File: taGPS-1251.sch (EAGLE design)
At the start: 84 parts, among them IC1 MSP430FR698X(1)80-PIN_PN, IC3 FT232RL

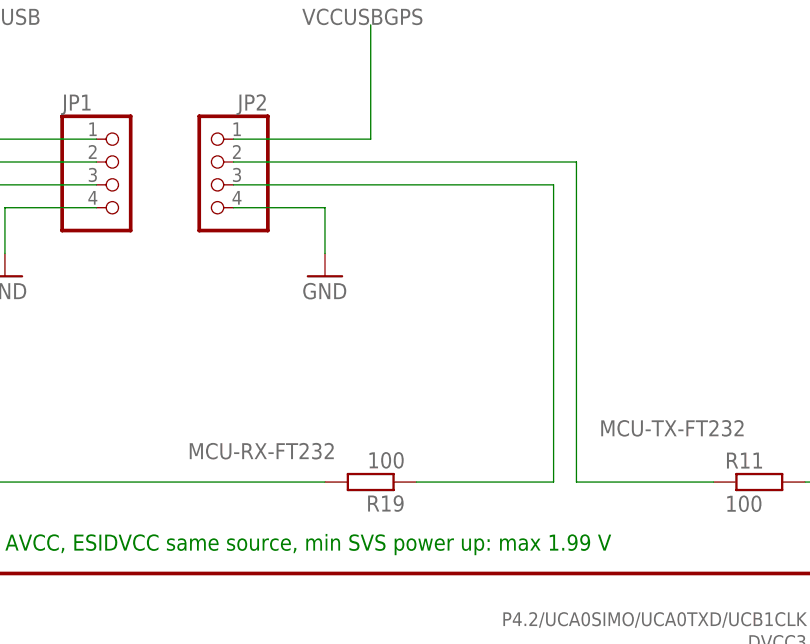
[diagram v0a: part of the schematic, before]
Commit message: Fix MCU RX/TX pinheader position, polish boards
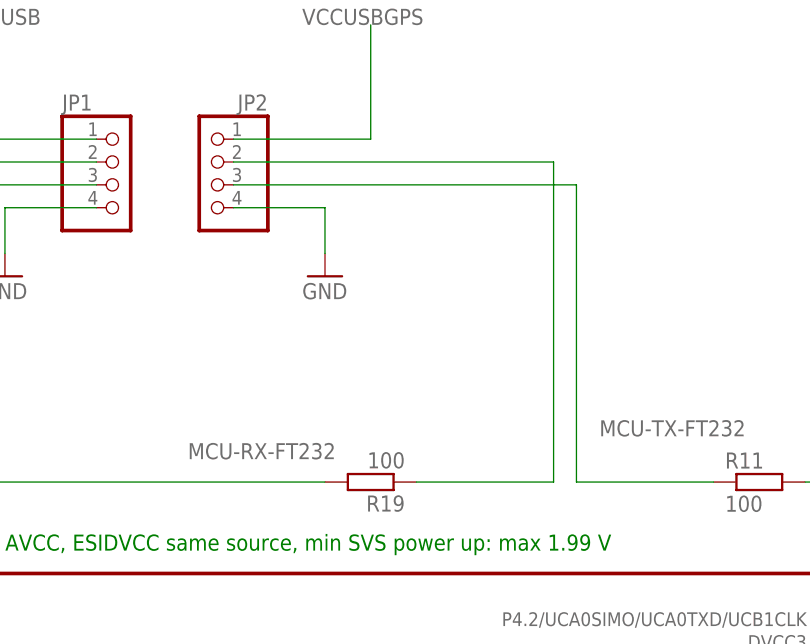
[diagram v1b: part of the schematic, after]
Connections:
- net MCU-TX-FT232: now also JP2.3; no longer JP2.2
- net N$8: now also JP2.2; no longer JP2.3
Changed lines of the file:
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@@
 <label x="-38.1" y="45.72" size="1.778" layer="95"/>
 <wire x1="-25.4" y1="40.64" x2="-40.64" y2="40.64" width="0.1524" layer="91"/>
-<wire x1="-40.64" y1="40.64" x2="-40.64" y2="76.2" width="0.1524" layer="91"/>
-<pinref part="JP2" gate="A" pin="2"/>
-<wire x1="-40.64" y1="76.2" x2="-78.74" y2="76.2" width="0.1524" layer="91"/>
+<wire x1="-40.64" y1="40.64" x2="-40.64" y2="73.66" width="0.1524" layer="91"/>
+<pinref part="JP2" gate="A" pin="3"/>
+<wire x1="-78.74" y1="73.66" x2="-40.64" y2="73.66" width="0.1524" layer="91"/>
 </segment>
 </net>
@@
 <pinref part="R19" gate="G$1" pin="1"/>
 <wire x1="-58.42" y1="40.64" x2="-43.18" y2="40.64" width="0.1524" layer="91"/>
-<wire x1="-43.18" y1="40.64" x2="-43.18" y2="73.66" width="0.1524" layer="91"/>
-<pinref part="JP2" gate="A" pin="3"/>
-<wire x1="-43.18" y1="73.66" x2="-78.74" y2="73.66" width="0.1524" layer="91"/>
-</segment>
-</net>
+<wire x1="-43.18" y1="40.64" x2="-43.18" y2="76.2" width="0.1524" layer="91"/>
+<pinref part="JP2" gate="A" pin="2"/>
+<wire x1="-43.18" y1="76.2" x2="-78.74" y2="76.2" width="0.1524" layer="91"/>
+</segment>
+</net>

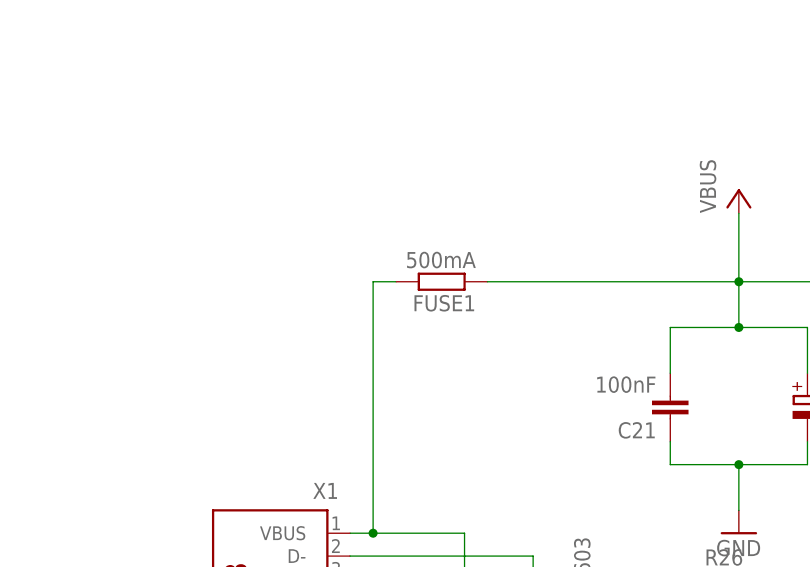
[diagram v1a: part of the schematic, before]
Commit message: Replace FUSE package to 1812
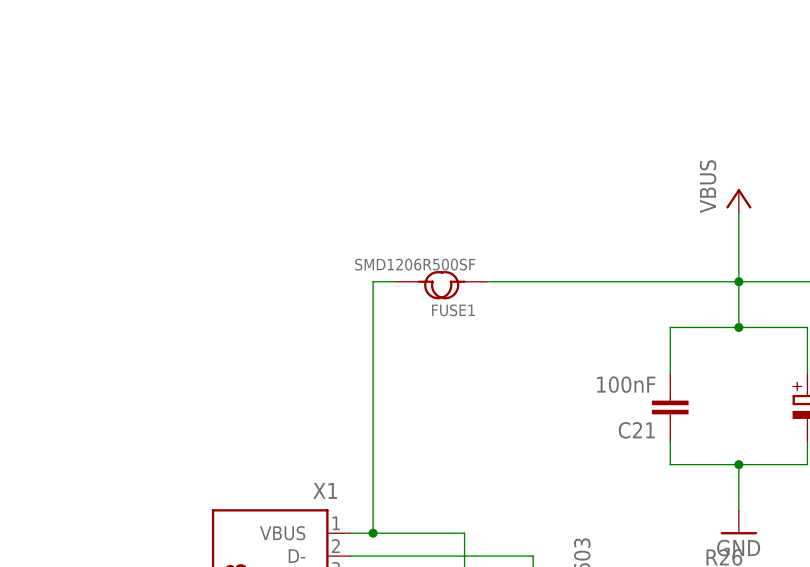
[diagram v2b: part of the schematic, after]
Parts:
- FUSE1: value 500mA -> SMD1206R500SF; device tagps:R-EU_R0805 -> tagps:SMD-PPTC-500MA-15V(1812)
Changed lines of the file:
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@@
 <layer number="48" name="Document" color="7" fill="1" visible="no" active="no"/>
 <layer number="49" name="Reference" color="7" fill="1" visible="no" active="no"/>
+<layer number="50" name="dxf" color="7" fill="1" visible="no" active="no"/>
 <layer number="51" name="tDocu" color="7" fill="1" visible="no" active="no"/>
 <layer number="52" name="bDocu" color="7" fill="1" visible="no" active="no"/>
+<layer number="53" name="tGND_GNDA" color="7" fill="9" visible="no" active="no"/>
+<layer number="54" name="bGND_GNDA" color="1" fill="9" visible="no" active="no"/>
+<layer number="56" name="wert" color="7" fill="1" visible="no" active="no"/>
+<layer number="57" name="tCAD" color="7" fill="1" visible="no" active="no"/>
 <layer number="90" name="Modules" color="5" fill="1" visible="yes" active="yes"/>
 <layer number="91" name="Nets" color="2" fill="1" visible="yes" active="yes"/>
@@
 <layer number="98" name="Guide" color="6" fill="1" visible="yes" active="yes"/>
 <layer number="99" name="SpiceOrder" color="5" fill="1" visible="yes" active="yes"/>
+<layer number="100" name="Muster" color="7" fill="1" visible="no" active="no"/>
+<layer number="101" name="Patch_Top" color="12" fill="4" visible="no" active="no"/>
+<layer number="102" name="Vscore" color="7" fill="1" visible="no" active="no"/>
+<layer number="103" name="tMap" color="7" fill="1" visible="no" active="no"/>
+<layer number="104" name="Name" color="7" fill="1" visible="no" active="no"/>
+<layer number="105" name="tPlate" color="7" fill="1" visible="no" active="no"/>
+<layer number="106" name="bPlate" color="7" fill="1" visible="no" active="no"/>
+<layer number="107" name="Crop" color="7" fill="1" visible="no" active="no"/>
+<layer number="108" name="fp8" color="7" fill="1" visible="yes" active="yes"/>
+<layer number="109" name="fp9" color="7" fill="1" visible="yes" active="yes"/>
+<layer number="110" name="110" color="7" fill="1" visible="yes" active="yes"/>
+<layer number="111" name="111" color="7" fill="1" visible="yes" active="yes"/>
+<layer number="112" name="tSilk" color="7" fill="1" visible="yes" active="yes"/>
+<layer number="113" name="IDFDebug" color="7" fill="1" visible="yes" active="yes"/>
+<layer number="114" name="FRNTMAAT1" color="7" fill="1" visible="no" active="no"/>
+<layer number="115" name="FRNTMAAT2" color="7" fill="1" visible="no" active="no"/>
+<layer number="116" name="Patch_BOT" color="9" fill="4" visible="no" active="no"/>
+<layer number="117" name="BACKMAAT1" color="7" fill="1" visible="no" active="no"/>
+<layer number="118" name="Rect_Pads" color="7" fill="1" visible="yes" active="yes"/>
+<layer number="119" name="KAP_TEKEN" color="7" fill="1" visible="no" active="no"/>
+<layer number="120" name="KAP_MAAT1" color="7" fill="1" visible="no" active="no"/>
+<layer number="121" name="_tsilk" color="7" fill="1" visible="no" active="no"/>
+<layer number="122" name="_bsilk" color="7" fill="1" visible="no" active="no"/>
+<layer number="123" name="tTestmark" color="7" fill="1" visible="yes" active="yes"/>
+<layer number="124" name="bTestmark" color="7" fill="1" visible="yes" active="yes"/>
+<layer number="125" name="_tNames" color="7" fill="1" visible="yes" active="yes"/>
+<layer number="126" name="_bNames" color="7" fill="1" visible="yes" active="yes"/>
+<layer number="127" name="_tValues" color="7" fill="1" visible="yes" active="yes"/>
+<layer number="128" name="_bValues" color="7" fill="1" visible="yes" active="yes"/>
+<layer number="130" name="SMDSTROOK" color="7" fill="1" visible="no" active="no"/>
+<layer number="131" name="tAdjust" color="7" fill="1" visible="yes" active="yes"/>
+<layer number="132" name="bAdjust" color="7" fill="1" visible="yes" active="yes"/>
+<layer number="144" name="DrillLegend" color="7" fill="1" visible="no" active="no"/>
+<layer number="150" name="Notes" color="7" fill="1" visible="yes" active="yes"/>
+<layer number="151" name="HeatSink" color="14" fill="1" visible="no" active="no"/>
+<layer number="152" name="_bDocu" color="7" fill="1" visible="yes" active="yes"/>
+<layer number="153" name="FabDoc1" color="6" fill="1" visible="no" active="no"/>
+<layer number="154" name="FabDoc2" color="2" fill="1" visible="no" active="no"/>
+<layer number="155" name="FabDoc3" color="7" fill="15" visible="no" active="no"/>
+<layer number="199" name="Contour" color="7" fill="1" visible="yes" active="yes"/>
+<layer number="200" name="200bmp" color="1" fill="10" visible="no" active="no"/>
+<layer number="201" name="201bmp" color="2" fill="1" visible="no" active="no"/>
+<layer number="202" name="202bmp" color="3" fill="1" visible="no" active="no"/>
+<layer number="203" name="203bmp" color="4" fill="10" visible="no" active="no"/>
+<layer number="204" name="204bmp" color="5" fill="10" visible="no" active="no"/>
+<layer number="205" name="205bmp" color="6" fill="10" visible="no" active="no"/>
+<layer number="206" name="206bmp" color="7" fill="10" visible="no" active="no"/>
+<layer number="207" name="207bmp" color="15" fill="10" visible="no" active="no"/>
+<layer number="208" name="208bmp" color="9" fill="10" visible="no" active="no"/>
+<layer number="209" name="209bmp" color="7" fill="1" visible="no" active="no"/>
+<layer number="210" name="210bmp" color="7" fill="1" visible="no" active="no"/>
+<layer number="211" name="211bmp" color="7" fill="1" visible="no" active="no"/>
+<layer number="212" name="212bmp" color="7" fill="1" visible="no" active="no"/>
+<layer number="213" name="213bmp" color="7" fill="1" visible="no" active="no"/>
+<layer number="214" name="214bmp" color="7" fill="1" visible="no" active="no"/>
+<layer number="215" name="215bmp" color="7" fill="1" visible="no" active="no"/>
+<layer number="216" name="216bmp" color="7" fill="1" visible="no" active="no"/>
+<layer number="217" name="217bmp" color="18" fill="1" visible="no" active="no"/>
+<layer number="218" name="218bmp" color="19" fill="1" visible="no" active="no"/>
+<layer number="219" name="219bmp" color="20" fill="1" visible="no" active="no"/>
+<layer number="220" name="220bmp" color="21" fill="1" visible="no" active="no"/>
+<layer number="221" name="221bmp" color="22" fill="1" visible="no" active="no"/>
+<layer number="222" name="222bmp" color="23" fill="1" visible="no" active="no"/>
+<layer number="223" name="223bmp" color="24" fill="1" visible="no" active="no"/>
+<layer number="224" name="224bmp" color="25" fill="1" visible="no" active="no"/>
+<layer number="225" name="225bmp" color="7" fill="1" visible="yes" active="yes"/>
+<layer number="226" name="226bmp" color="7" fill="1" visible="yes" active="yes"/>
+<layer number="227" name="227bmp" color="7" fill="1" visible="yes" active="yes"/>
+<layer number="228" name="228bmp" color="7" fill="1" visible="yes" active="yes"/>
+<layer number="230" name="230bmp" color="7" fill="1" visible="yes" active="yes"/>
+<layer number="231" name="Eagle3D_PG1" color="7" fill="1" visible="no" active="no"/>
+<layer number="232" name="Eagle3D_PG2" color="7" fill="1" visible="no" active="no"/>
+<layer number="233" name="Eagle3D_PG3" color="7" fill="1" visible="no" active="no"/>
+<layer number="248" name="Housing" color="7" fill="1" visible="yes" active="yes"/>
+<layer number="249" name="Edge" color="7" fill="1" visible="yes" active="yes"/>
+<layer number="250" name="Descript" color="3" fill="1" visible="no" active="no"/>
+<layer number="251" name="SMDround" color="12" fill="11" visible="no" active="no"/>
+<layer number="254" name="OrgLBR" color="13" fill="1" visible="no" active="no"/>
+<layer number="255" name="Accent" color="7" fill="1" visible="no" active="no"/>
 </layers>
 <schematic xreflabel="%F%N/%S.%C%R" xrefpart="/%S.%C%R">
@@
 <classes>
 <class number="0" name="signal" width="0.254" drill="0.254">
-<clearance class="0" value="0.1"/>
+<clearance class="0" value="0.15"/>
 </class>
 <class number="1" name="charimp50" width="0.254" drill="0.254">
-<clearance class="1" value="0.1"/>
+<clearance class="1" value="0.15"/>
 </class>
 <class number="2" name="conect" width="0.254" drill="0.254">
@@
 <part name="R30" library="tagps" deviceset="R-EU_" device="R0603" value="100"/>
 <part name="R31" library="tagps" deviceset="R-EU_" device="R0603" value="100"/>
-<part name="FUSE1" library="tagps" deviceset="R-EU_" device="R0805" value="500mA"/>
+<part name="FUSE1" library="tagps" deviceset="SMD-PPTC-500MA-15V(1812)" device="" value="SMD1206R500SF"/>
 <part name="VAR1" library="tagps" deviceset="VARISTOR" device="CN0603"/>
 <part name="VAR2" library="tagps" deviceset="VARISTOR" device="CN0603"/>
